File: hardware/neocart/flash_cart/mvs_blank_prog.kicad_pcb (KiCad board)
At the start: 2 copper layers, 174 x 134 mm, 120 parts

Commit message: Remove orphan pin number markers (1, 30, 60) from both boards
Co-Authored-By: Claude Opus 4.6 (1M context) <noreply@anthropic.com>
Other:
- board text removed: "1"
- board text removed: "30"
- board text removed: "60"
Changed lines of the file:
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@@
 		(layer "Edge.Cuts")
-	)
-	(gr_text "60"
-		(at 63 148 0)
-		(layer "F.SilkS")
-		(effects
-			(font
-				(size 1.17 1.17)
-				(thickness 0.15)
-			)
-		)
-	)
-	(gr_text "30"
-		(at 141 148 0)
-		(layer "F.SilkS")
-		(effects
-			(font
-				(size 1.17 1.17)
-				(thickness 0.15)
-			)
-		)
-	)
-	(gr_text "1"
-		(at 216 148 0)
-		(layer "F.SilkS")
-		(effects
-			(font
-				(size 1.17 1.17)
-				(thickness 0.15)
-			)
-		)
 	)
 	(gr_text "GND"

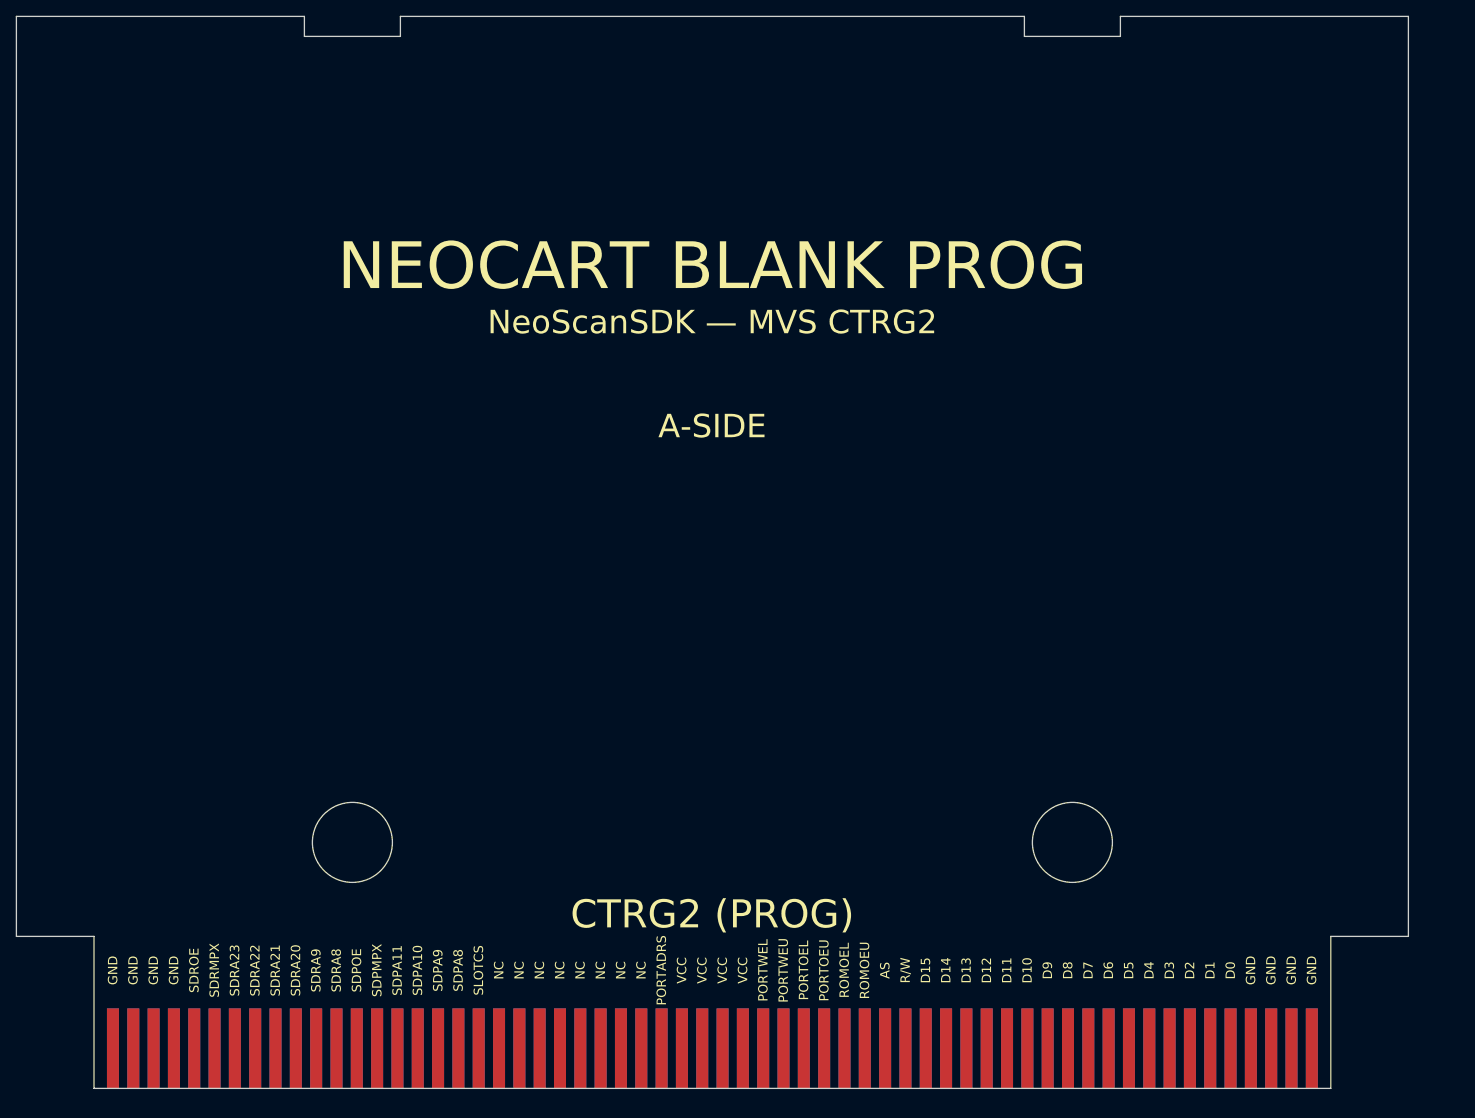
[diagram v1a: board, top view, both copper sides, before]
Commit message: PROG board: P-ROM 2x20 header + routing WIP, viewer mirroring fix
- P-ROM header on right side, 2x20 (40 pins), labeled both sides
- Pins sorted by gold finger position for monotonic fan-out
- Routing: F.Cu for A-side signals, B.Cu for B-side, 40 crossings remain (WIP)
- build_prog.py: full board rebuild script
- Viewer: back views now use --mirror for correct physical orientation
- B.SilkS text mirroring fixed on both PROG and CHA boards

Co-Authored-By: Claude Opus 4.6 (1M context) <noreply@anthropic.com>
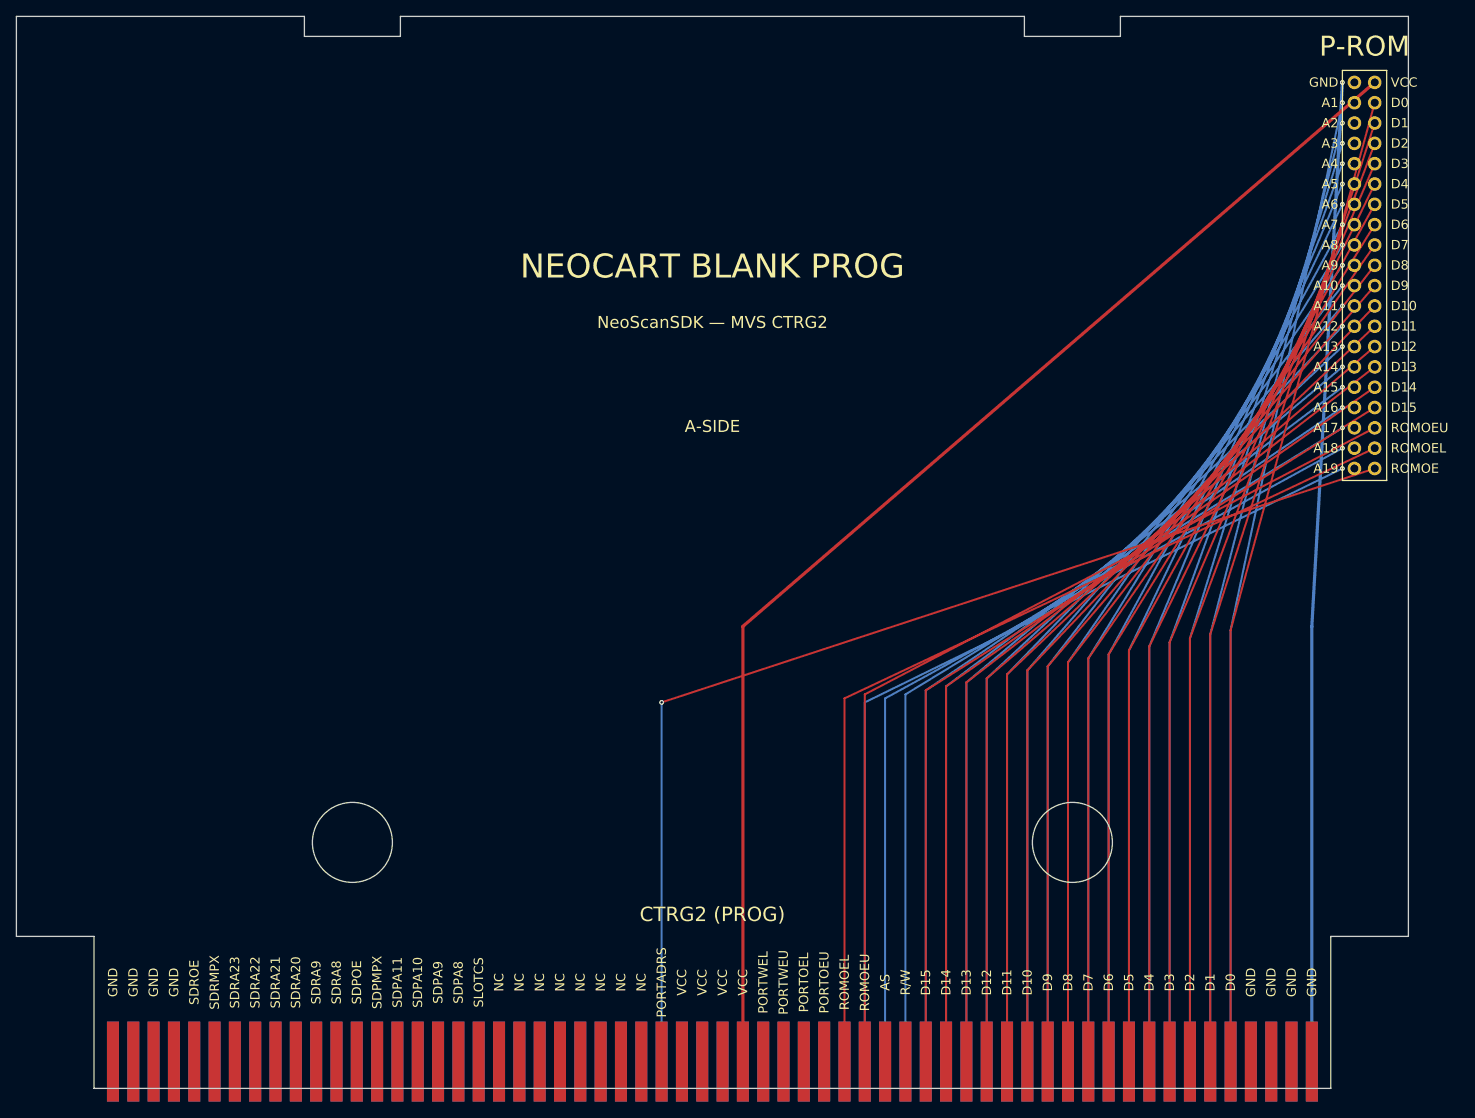
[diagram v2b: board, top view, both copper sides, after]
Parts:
- added J_PROM: P-ROM 2x20, , F.Cu at (220.0, 32.0)
- moved A1 1.65 mm to (214.7, 154.4)
- moved A10 1.65 mm to (191.8, 154.4)
- moved A11 1.65 mm to (189.3, 154.4)
- moved A12 1.65 mm to (186.7, 154.4)
- moved A13 1.65 mm to (184.2, 154.4)
- moved A14 1.65 mm to (181.7, 154.4)
- moved A15 1.65 mm to (179.1, 154.4)
- moved A16 1.65 mm to (176.6, 154.4)
- moved A17 1.65 mm to (174.0, 154.4)
- moved A18 1.65 mm to (171.5, 154.4)
- moved A19 1.65 mm to (169.0, 154.4)
- moved A2 1.65 mm to (212.1, 154.4)
- moved A20 1.65 mm to (166.4, 154.4)
- moved A21 1.65 mm to (163.9, 154.4)
- moved A22 1.65 mm to (161.3, 154.4)
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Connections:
- A1 pad 1: (no net) -> GND
- A10 pad 1: (no net) -> D5
- A11 pad 1: (no net) -> D6
- A12 pad 1: (no net) -> D7
- A13 pad 1: (no net) -> D8
- A14 pad 1: (no net) -> D9
- A15 pad 1: (no net) -> D10
- A16 pad 1: (no net) -> D11
- A17 pad 1: (no net) -> D12
- A18 pad 1: (no net) -> D13
- A19 pad 1: (no net) -> D14
- A2 pad 1: (no net) -> GND
- A20 pad 1: (no net) -> D15
- A21 pad 1: (no net) -> R/W
- A22 pad 1: (no net) -> AS
- A23 pad 1: (no net) -> ROMOEU
- A24 pad 1: (no net) -> ROMOEL
- A25 pad 1: (no net) -> PORTOEU
- A26 pad 1: (no net) -> PORTOEL
- A27 pad 1: (no net) -> PORTWEU
- A28 pad 1: (no net) -> PORTWEL
- A29 pad 1: (no net) -> VCC
- A3 pad 1: (no net) -> GND
- A30 pad 1: (no net) -> VCC
- A31 pad 1: (no net) -> VCC
- A32 pad 1: (no net) -> VCC
- A33 pad 1: (no net) -> PORTADRS
- A4 pad 1: (no net) -> GND
- A42 pad 1: (no net) -> SLOTCS
- A43 pad 1: (no net) -> SDPA8
- A44 pad 1: (no net) -> SDPA9
- A45 pad 1: (no net) -> SDPA10
- A46 pad 1: (no net) -> SDPA11
- A47 pad 1: (no net) -> SDPMPX
- A48 pad 1: (no net) -> SDPOE
- A49 pad 1: (no net) -> SDRA8
- A5 pad 1: (no net) -> D0
- A50 pad 1: (no net) -> SDRA9
- A51 pad 1: (no net) -> SDRA20
- A52 pad 1: (no net) -> SDRA21
- A53 pad 1: (no net) -> SDRA22
- A54 pad 1: (no net) -> SDRA23
- A55 pad 1: (no net) -> SDRMPX
- A56 pad 1: (no net) -> SDROE
- A57 pad 1: (no net) -> GND
- A58 pad 1: (no net) -> GND
- A59 pad 1: (no net) -> GND
- A6 pad 1: (no net) -> D1
- A60 pad 1: (no net) -> GND
- A7 pad 1: (no net) -> D2
- A8 pad 1: (no net) -> D3
- A9 pad 1: (no net) -> D4
- B1 pad 1: (no net) -> GND
- B10 pad 1: (no net) -> A6
- B11 pad 1: (no net) -> A7
- B12 pad 1: (no net) -> A8
- B13 pad 1: (no net) -> A9
- B14 pad 1: (no net) -> A10
- B15 pad 1: (no net) -> A11
- B16 pad 1: (no net) -> A12
- B17 pad 1: (no net) -> A13
- B18 pad 1: (no net) -> A14
- B19 pad 1: (no net) -> A15
- B2 pad 1: (no net) -> GND
- B20 pad 1: (no net) -> A16
- B21 pad 1: (no net) -> A17
- B22 pad 1: (no net) -> A18
- B23 pad 1: (no net) -> A19
- B24 pad 1: (no net) -> 68KCLKB
- B25 pad 1: (no net) -> ROMWAIT
- B26 pad 1: (no net) -> PWAIT0
- B27 pad 1: (no net) -> PWAIT1
- B28 pad 1: (no net) -> PDTACK
- B29 pad 1: (no net) -> VCC
- B3 pad 1: (no net) -> GND
- B30 pad 1: (no net) -> VCC
- B31 pad 1: (no net) -> VCC
- B32 pad 1: (no net) -> VCC
- B33 pad 1: (no net) -> ROMOE
- B34 pad 1: (no net) -> 4MB
- B35 pad 1: (no net) -> RESET
- B4 pad 1: (no net) -> GND
- B41 pad 1: (no net) -> SDPAD0
- B42 pad 1: (no net) -> SDPAD1
- B43 pad 1: (no net) -> SDPAD2
- B44 pad 1: (no net) -> SDPAD3
- B45 pad 1: (no net) -> SDPAD4
- B46 pad 1: (no net) -> SDPAD5
- B47 pad 1: (no net) -> SDPAD6
- B48 pad 1: (no net) -> SDPAD7
- B49 pad 1: (no net) -> SDRAD0
- B5 pad 1: (no net) -> A1
- B50 pad 1: (no net) -> SDRAD1
- B51 pad 1: (no net) -> SDRAD2
- B52 pad 1: (no net) -> SDRAD3
- B53 pad 1: (no net) -> SDRAD4
- B54 pad 1: (no net) -> SDRAD5
- B55 pad 1: (no net) -> SDRAD6
- B56 pad 1: (no net) -> SDRAD7
- B57 pad 1: (no net) -> GND
- B58 pad 1: (no net) -> GND
- B59 pad 1: (no net) -> GND
- B6 pad 1: (no net) -> A2
- B60 pad 1: (no net) -> GND
- B7 pad 1: (no net) -> A3
- B8 pad 1: (no net) -> A4
- B9 pad 1: (no net) -> A5
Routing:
- net VCC: track 0.00 -> 158.6 mm
- net ROMOE: track 0.00 -> 138.7 mm, vias 0 -> 1
- net GND: track 0.00 -> 122.5 mm, vias 0 -> 1
- net D0: track 0.00 -> 122.3 mm
- net A1: track 0.00 -> 121.3 mm, vias 0 -> 1
- net D1: track 0.00 -> 120.5 mm
- net A2: track 0.00 -> 119.4 mm, vias 0 -> 1
- net D2: track 0.00 -> 119.0 mm
- net ROMOEL: track 0.00 -> 118.7 mm
- net ROMOEU: track 0.00 -> 117.8 mm
- net A3: track 0.00 -> 117.6 mm, vias 0 -> 1
- net D3: track 0.00 -> 117.5 mm
- net D4: track 0.00 -> 116.2 mm
- net A4: track 0.00 -> 116.0 mm, vias 0 -> 1
- net D5: track 0.00 -> 115.1 mm
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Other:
- board text added: "P-ROM"

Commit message: NeoCart hardware work, tools and examples from earlier sessions; .gitignore for local tooling
- hardware/neocart: the board generators, KiCad projects and boards (PROG v3, P board, programmer, blank boards,
  adapters, flash cart, production), footprints, Verilog, firmware sources, simulation sources, Gerbers / BOM / CPL,
  renders and docs (FPGA_DESIGN, BOM, HANDOFF_FINAL, pin maps)
- tools/pcb_engine; KOF95 capture logs; danmaku test scripts; hello_neo's Furnace song; the SoccerFury player source;
  the tracked demo ROMs rebuilt; CLAUDE.md updates
- .gitignore: AppDir / squashfs-root / node_modules, the nested mame and neosdk repos, the kicad-mcp-server clone,
  vendor datasheets, 3D models, KiCad backups / history / locks / per-machine state, logs, simulator and firmware
  builds, new ROM builds, and the routing runs' intermediate boards

Co-Authored-By: Claude Opus 5.5 <noreply@anthropic.com>
Claude-Session: https://claude.ai/code/session_01XhxN754ESQrKXnzjnRdvPt
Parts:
- A21: value R/W -> R_W
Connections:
- net R/W renamed R_W
- A1 pad 1: GND -> GND_A1
- A2 pad 1: GND -> GND_A2
- A3 pad 1: GND -> GND_A3
- A30 pad 1: VCC -> VCC_A30
- A31 pad 1: VCC -> VCC_A31
- A32 pad 1: VCC -> VCC_A32
- A4 pad 1: GND -> GND_A4
- A57 pad 1: GND -> GND_A57
- A58 pad 1: GND -> GND_A58
- A59 pad 1: GND -> GND_A59
- A60 pad 1: GND -> GND_A60
- B2 pad 1: GND -> GND_B2
- B29 pad 1: VCC -> VCC_B29
- B3 pad 1: GND -> GND_B3
- B30 pad 1: VCC -> VCC_B30
- B31 pad 1: VCC -> VCC_B31
- B32 pad 1: VCC -> VCC_B32
- B4 pad 1: GND -> GND_B4
- B57 pad 1: GND -> GND_B57
- B58 pad 1: GND -> GND_B58
- B59 pad 1: GND -> GND_B59
- B60 pad 1: GND -> GND_B60
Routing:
- net VCC: track 158.6 -> 0.00 mm
- net ROMOE: track 138.7 -> 0.00 mm, vias 1 -> 0
- net GND: track 122.5 -> 0.00 mm, vias 1 -> 0
- net D0: track 122.3 -> 0.00 mm
- net A1: track 121.3 -> 0.00 mm, vias 1 -> 0
- net D1: track 120.5 -> 0.00 mm
- net A2: track 119.4 -> 0.00 mm, vias 1 -> 0
- net D2: track 119.0 -> 0.00 mm
- net ROMOEL: track 118.7 -> 0.00 mm
- net ROMOEU: track 117.8 -> 0.00 mm
- net A3: track 117.6 -> 0.00 mm, vias 1 -> 0
- net D3: track 117.5 -> 0.00 mm
- net D4: track 116.2 -> 0.00 mm
- net A4: track 116.0 -> 0.00 mm, vias 1 -> 0
- net D5: track 115.1 -> 0.00 mm
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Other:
- board text added: "NEOCART PROG"
- board text added: "R_W"
- board text removed: "NEOCART BLANK PROG"
- board text removed: "NeoScanSDK — MVS CTRG2"
- board text removed: "R/W"
